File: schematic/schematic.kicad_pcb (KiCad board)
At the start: 4 copper layers, 100 x 100 mm, 260 parts, among them J1 Conn_01x04, J10 Conn_01x03, J11 Conn_01x02, J12 Conn_01x02, J13 Conn_01x02, J14 Conn_01x02, J15 Conn_01x02, J16 Conn_01x02, J17 Conn_01x04, J18 Conn_02x13_Odd_Even, J2 Conn_01x04, J3 Conn_01x04, J4 Conn_01x04, J5 Conn_01x04, J6 Conn_01x06, J7 Conn_01x03, J8 Screw_Terminal_01x02, J9 Conn_01x03, Q1 PSMN1R7-30YL, Q2 PSMN1R7-30YL, Q3 NCV8402, Q4 NCV8402, SW1 SW_Push_Dual, SW2 SW_DIP_x03, U1 STM32F401VETx, U2 TMC2130, U3 TMC2130, U4 TMC2130, U5 TMC2130, U6 BD9E302EFJ, U7 BD9E302EFJ, U8 BD9E302EFJ, Y1 Crystal_GND24

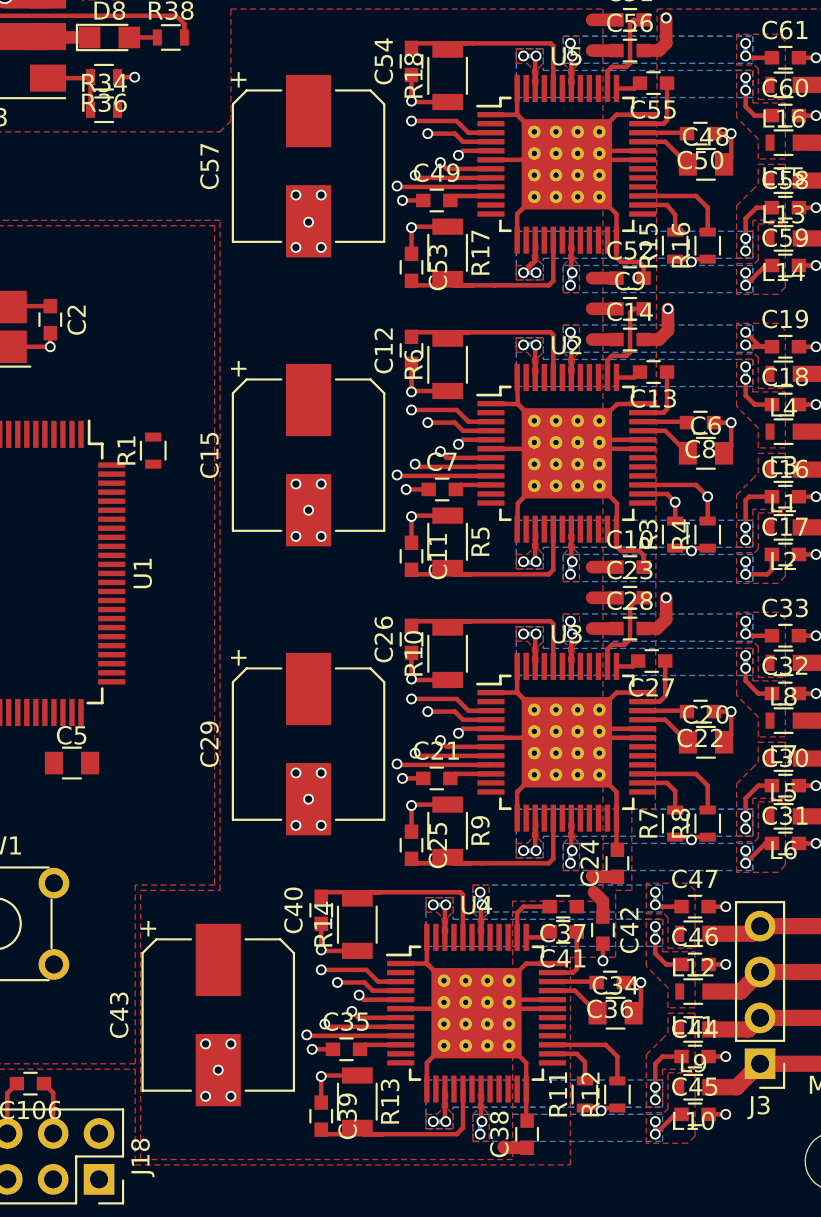
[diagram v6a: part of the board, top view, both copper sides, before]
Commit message: routed 3.3V power and start re arange signals
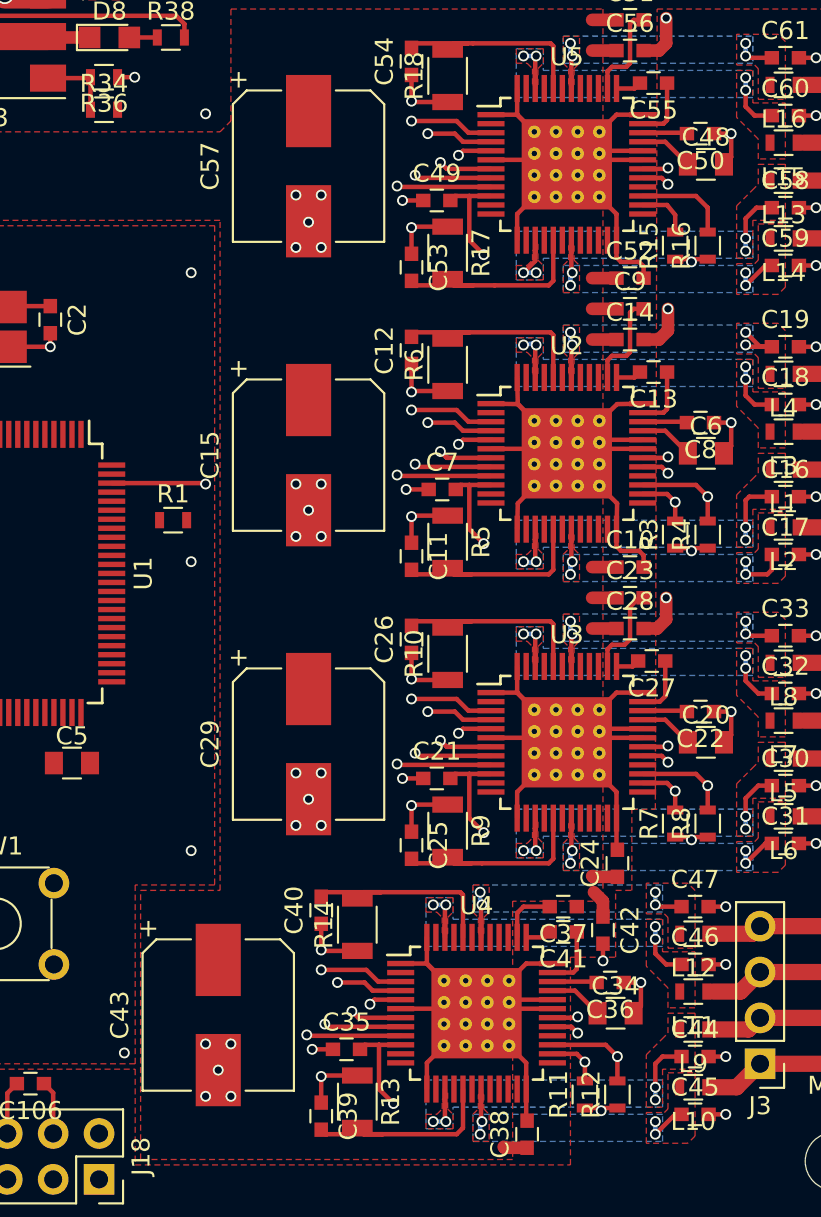
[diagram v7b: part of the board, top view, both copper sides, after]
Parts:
- moved R1 4.00 mm to (224.8, 110.9), turned to 0 degrees
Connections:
- J18 pad 1: (no net) -> Net-(J18-Pad1)
- J18 pad 12: (no net) -> Net-(J18-Pad12)
- J18 pad 16: (no net) -> Net-(J18-Pad16)
- J18 pad 17: (no net) -> Net-(J18-Pad17)
- J18 pad 18: (no net) -> Net-(J18-Pad18)
- J18 pad 19: (no net) -> Net-(J18-Pad19)
- J18 pad 21: (no net) -> Net-(J18-Pad21)
- J18 pad 22: (no net) -> Net-(J18-Pad22)
- J18 pad 23: (no net) -> Net-(J18-Pad23)
- J18 pad 24: (no net) -> Net-(J18-Pad24)
- J18 pad 26: (no net) -> Net-(J18-Pad26)
- J18 pad 3: (no net) -> Net-(J18-Pad3)
- J18 pad 5: (no net) -> Net-(J18-Pad5)
- J18 pad 7: (no net) -> Net-(J18-Pad7)
- U1 pad 1: (no net) -> Net-(U1-Pad1)
- U1 pad 15: XEND -> Net-(U1-Pad15)
- U1 pad 16: YEND -> Net-(U1-Pad16)
- U1 pad 17: ZEND -> Net-(U1-Pad17)
- U1 pad 18: (no net) -> Net-(U1-Pad18)
- U1 pad 2: (no net) -> Net-(U1-Pad2)
- U1 pad 21: (no net) -> Net-(U1-Pad21)
- U1 pad 3: (no net) -> Net-(U1-Pad3)
- U1 pad 33: (no net) -> Net-(U1-Pad33)
- U1 pad 34: (no net) -> Net-(U1-Pad34)
- U1 pad 35: (no net) -> Net-(U1-Pad35)
- U1 pad 36: (no net) -> Net-(U1-Pad36)
- U1 pad 38: (no net) -> Net-(U1-Pad38)
- U1 pad 39: (no net) -> Net-(U1-Pad39)
- U1 pad 4: (no net) -> Net-(U1-Pad4)
- U1 pad 40: (no net) -> Net-(U1-Pad40)
- U1 pad 41: (no net) -> Net-(U1-Pad41)
- U1 pad 42: (no net) -> Net-(U1-Pad42)
- U1 pad 43: (no net) -> Net-(U1-Pad43)
- U1 pad 44: (no net) -> Net-(U1-Pad44)
- U1 pad 45: (no net) -> Net-(U1-Pad45)
- U1 pad 46: (no net) -> Net-(U1-Pad46)
- U1 pad 47: (no net) -> Net-(U1-Pad47)
- U1 pad 5: (no net) -> Net-(U1-Pad5)
- U1 pad 51: (no net) -> Net-(U1-Pad51)
- U1 pad 55: (no net) -> Net-(U1-Pad55)
- U1 pad 56: (no net) -> Net-(U1-Pad56)
- U1 pad 57: (no net) -> Net-(U1-Pad57)
- U1 pad 58: (no net) -> Net-(U1-Pad58)
- U1 pad 59: (no net) -> Net-(U1-Pad59)
- U1 pad 6: (no net) -> Net-(U1-Pad6)
- U1 pad 60: (no net) -> Net-(U1-Pad60)
- U1 pad 61: (no net) -> Net-(U1-Pad61)
- U1 pad 62: (no net) -> Net-(U1-Pad62)
- U1 pad 63: (no net) -> Net-(U1-Pad63)
- U1 pad 67: (no net) -> Net-(U1-Pad67)
- U1 pad 7: (no net) -> Net-(U1-Pad7)
- U1 pad 70: (no net) -> Net-(U1-Pad70)
- U1 pad 71: ESS -> Net-(U1-Pad71)
- U1 pad 72: ZSS -> Net-(U1-Pad72)
- U1 pad 76: XSS -> Net-(U1-Pad76)
- U1 pad 77: YSS -> Net-(U1-Pad77)
- U1 pad 78: EEN -> Net-(U1-Pad78)
- U1 pad 79: ED1 -> Net-(U1-Pad79)
- U1 pad 8: (no net) -> Net-(U1-Pad8)
- U1 pad 80: ED0 -> Net-(U1-Pad80)
- U1 pad 81: EDIR -> Net-(U1-Pad81)
- U1 pad 82: ESTEP -> Net-(U1-Pad82)
- U1 pad 83: ZEN -> Net-(U1-Pad83)
- U1 pad 84: ZD1 -> Net-(U1-Pad84)
- U1 pad 85: ZD0 -> Net-(U1-Pad85)
- U1 pad 86: ZDIR -> Net-(U1-Pad86)
- U1 pad 87: ZSTEP -> Net-(U1-Pad87)
- U1 pad 88: XEN -> Net-(U1-Pad88)
- U1 pad 89: XD1 -> Net-(U1-Pad89)
- U1 pad 9: (no net) -> Net-(U1-Pad9)
- U1 pad 90: XD0 -> Net-(U1-Pad90)
- U1 pad 91: XDIR -> Net-(U1-Pad91)
- U1 pad 92: XSTEP -> ED0
- U1 pad 93: YEN -> ED1
- U1 pad 95: YD1 -> EEN
- U1 pad 96: YD0 -> EDIR
- U1 pad 97: YDIR -> ESTEP
- U1 pad 98: YSTEP -> ESS
- U2 pad 12: (no net) -> Net-(U2-Pad12)
- U2 pad 2: (no net) -> Net-(U2-Pad2)
- U2 pad 23: (no net) -> Net-(U2-Pad23)
- U2 pad 25: (no net) -> Net-(U2-Pad25)
- U3 pad 12: (no net) -> Net-(U3-Pad12)
- U3 pad 2: (no net) -> Net-(U3-Pad2)
- U3 pad 23: (no net) -> Net-(U3-Pad23)
- U3 pad 25: (no net) -> Net-(U3-Pad25)
- U4 pad 12: (no net) -> Net-(U4-Pad12)
- U4 pad 2: (no net) -> Net-(U4-Pad2)
- U4 pad 23: (no net) -> Net-(U4-Pad23)
- U4 pad 25: (no net) -> Net-(U4-Pad25)
- U5 pad 12: (no net) -> Net-(U5-Pad12)
- U5 pad 2: (no net) -> Net-(U5-Pad2)
- U5 pad 23: (no net) -> Net-(U5-Pad23)
- U5 pad 25: (no net) -> Net-(U5-Pad25)
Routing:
- net +3V3: track 17.2 -> 146.7 mm, vias 4 -> 12
- net ESS: track 4.67 -> 42.0 mm, vias 1 -> 3
- net EEN: track 0.00 -> 17.8 mm, vias 0 -> 1
- net SCK: track 46.7 -> 63.8 mm
- net MOSI: track 43.7 -> 60.7 mm
- net MISO: track 40.1 -> 56.5 mm
- net /AREF/XY-REF: track 0.00 -> 2.84 mm, vias 0 -> 2
- net ZEN: track 0.00 -> 1.54 mm, vias 0 -> 1
- net YEN: track 0.00 -> 1.54 mm, vias 0 -> 1
- net XEN: track 0.00 -> 1.54 mm, vias 0 -> 1
- net /AREF/E-REF: track 0.00 -> 1.42 mm, vias 0 -> 1
- net /AREF/Z-REF: track 0.00 -> 1.42 mm, vias 0 -> 1
- net ZD1: vias 0 -> 1
- net ZD0: vias 0 -> 1
- net YD1: vias 0 -> 1
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
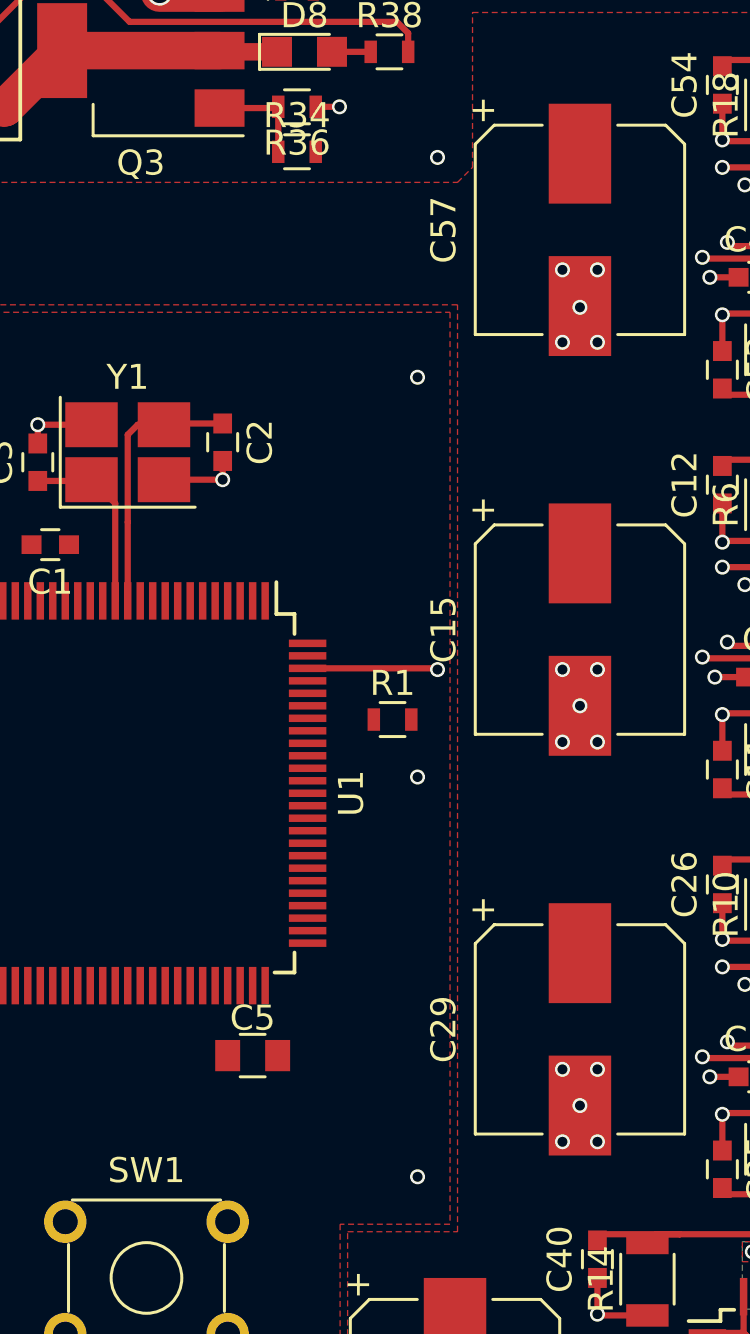
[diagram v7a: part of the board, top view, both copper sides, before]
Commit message: Reassigned signals to driver for easier routing
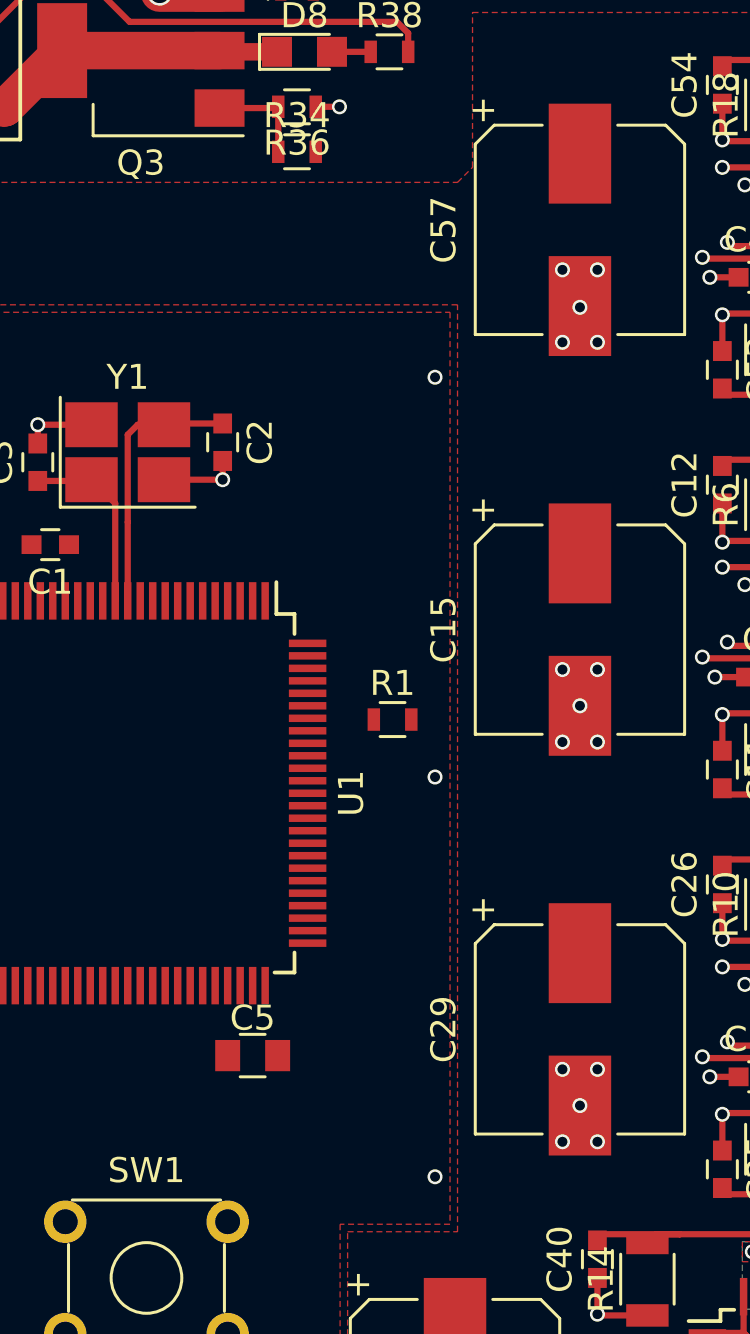
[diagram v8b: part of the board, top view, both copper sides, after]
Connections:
- U1 pad 71: Net-(U1-Pad71) -> ZD0
- U1 pad 72: Net-(U1-Pad72) -> ZD1
- U1 pad 76: Net-(U1-Pad76) -> ZEN
- U1 pad 77: Net-(U1-Pad77) -> ZDIR
- U1 pad 78: Net-(U1-Pad78) -> ZSTEP
- U1 pad 79: Net-(U1-Pad79) -> ZSS
- U1 pad 80: Net-(U1-Pad80) -> YD0
- U1 pad 81: Net-(U1-Pad81) -> YD1
- U1 pad 82: Net-(U1-Pad82) -> YEN
- U1 pad 83: Net-(U1-Pad83) -> YDIR
- U1 pad 84: Net-(U1-Pad84) -> YSTEP
- U1 pad 85: Net-(U1-Pad85) -> YSS
- U1 pad 86: Net-(U1-Pad86) -> XD0
- U1 pad 87: Net-(U1-Pad87) -> XD1
- U1 pad 88: Net-(U1-Pad88) -> XEN
- U1 pad 89: Net-(U1-Pad89) -> XDIR
- U1 pad 90: Net-(U1-Pad90) -> XSTEP
- U1 pad 91: Net-(U1-Pad91) -> XSS
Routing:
- net ESS: track 42.0 -> 4.67 mm, vias 3 -> 1
- net +3V3: track 146.7 -> 144.6 mm
